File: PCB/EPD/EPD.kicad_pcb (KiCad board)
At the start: 2 copper layers, 70 x 70 mm, 66 parts, among them J1 Conn_01x26, J2 Shelly, J3 USB-PROG, J4 BTN1, J6 BTN2, J7 USB-C-Socket-V, J8 PWR, P1 +, P10 2, P11 1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

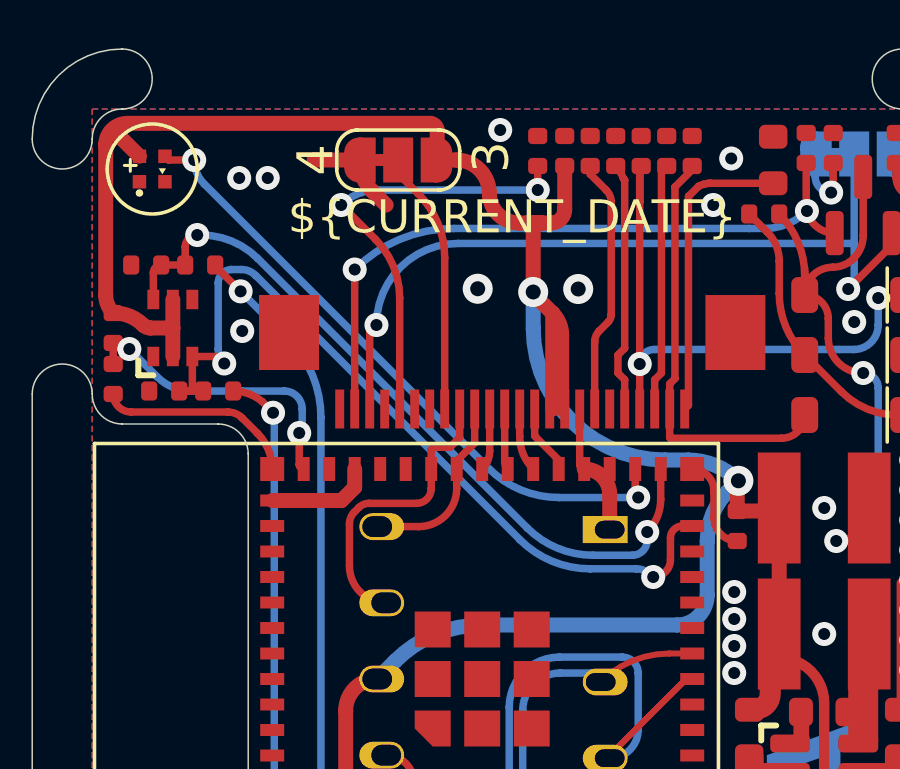
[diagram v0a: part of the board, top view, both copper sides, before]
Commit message: Moved connector and tidy GPIOs used
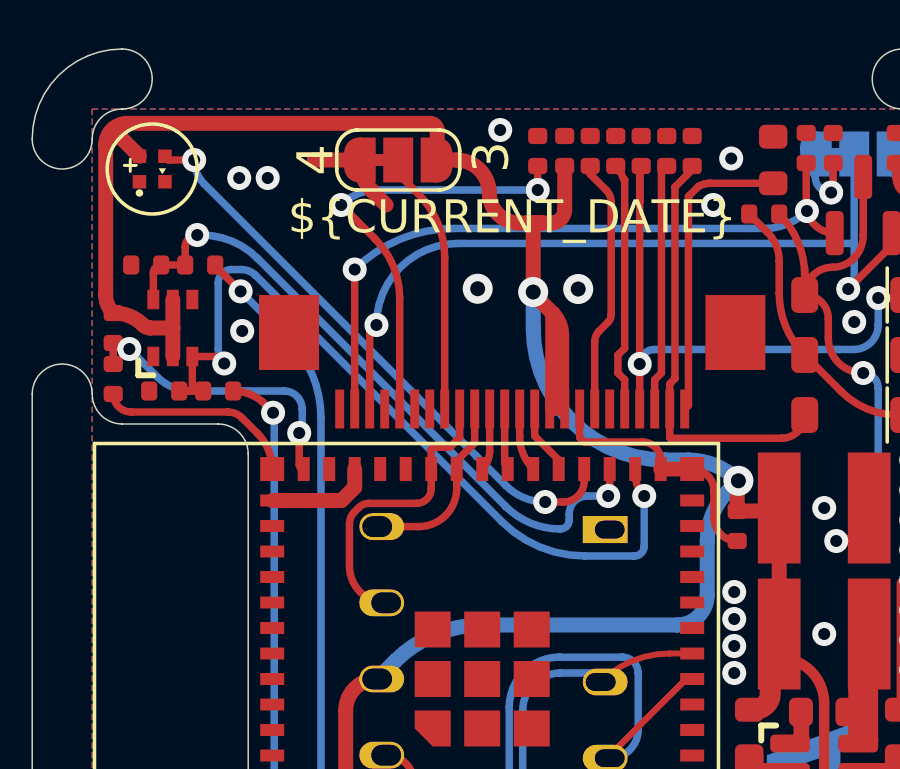
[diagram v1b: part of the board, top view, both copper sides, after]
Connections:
- U4 pad 29: BTN1 -> unconnected-(U4-GPIO34-Pad29)
- U4 pad 31: BTN2 -> GND
- U4 pad 32: RGB -> BTN1
- U4 pad 33: GND -> BTN2
- U4 pad 34: GND -> RGB
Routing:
- net BTN2: track 25.2 -> 22.4 mm
- net RGB: track 21.5 -> 19.6 mm
- net GND: track 21.3 -> 22.1 mm
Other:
- board text added: "43"
- board text added: "44"
- board text removed: "34"
- board text removed: "35"

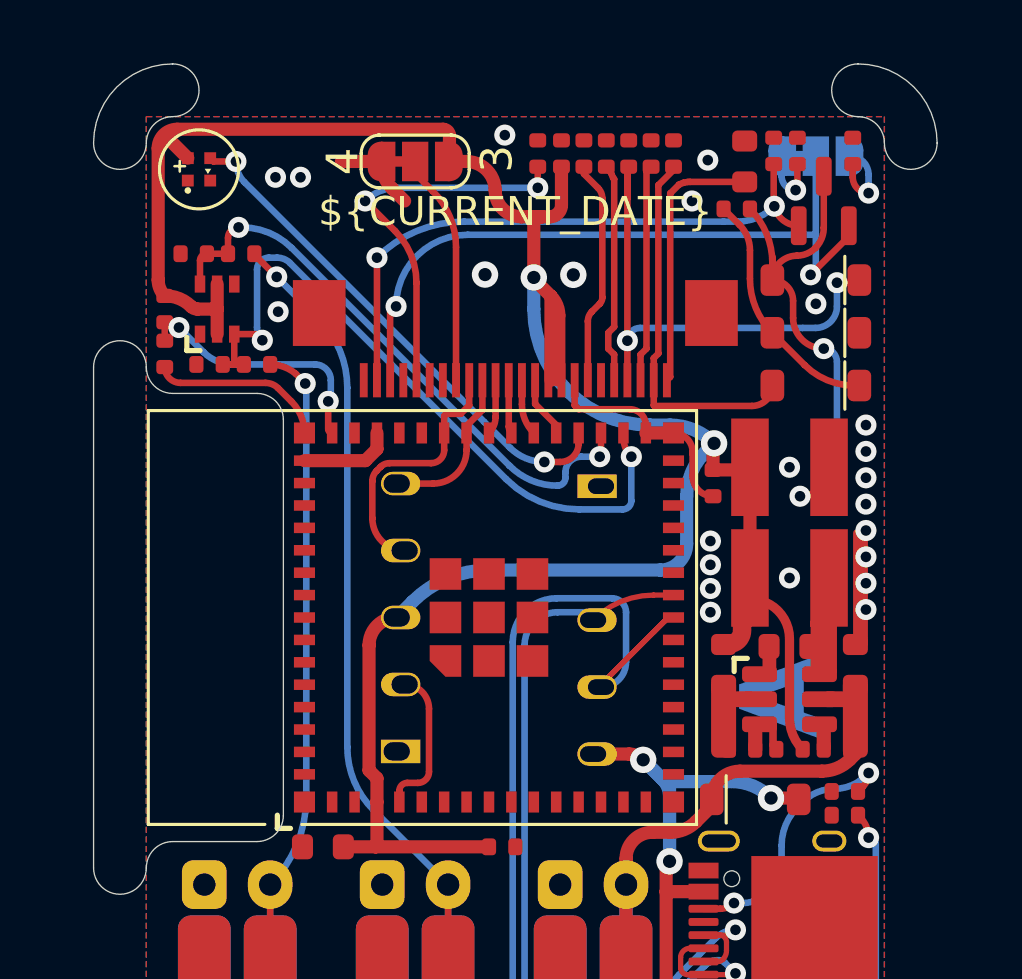
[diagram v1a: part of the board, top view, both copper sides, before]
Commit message: Moved connector to reduce slack
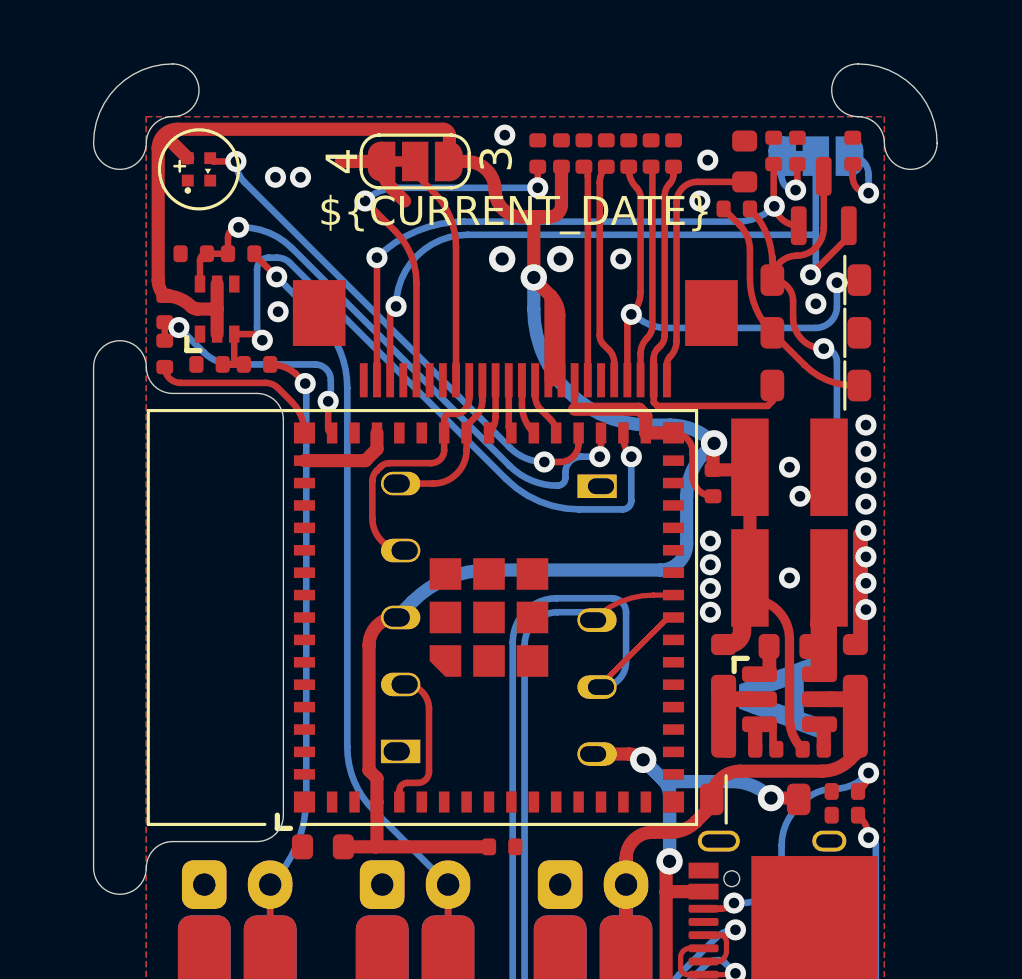
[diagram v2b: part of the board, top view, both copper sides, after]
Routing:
- net GND: track 22.1 -> 25.6 mm, vias 23 -> 24
- net Net-(D3-K): track 19.6 -> 18.2 mm
- net Net-(D2-A): track 14.2 -> 15.1 mm

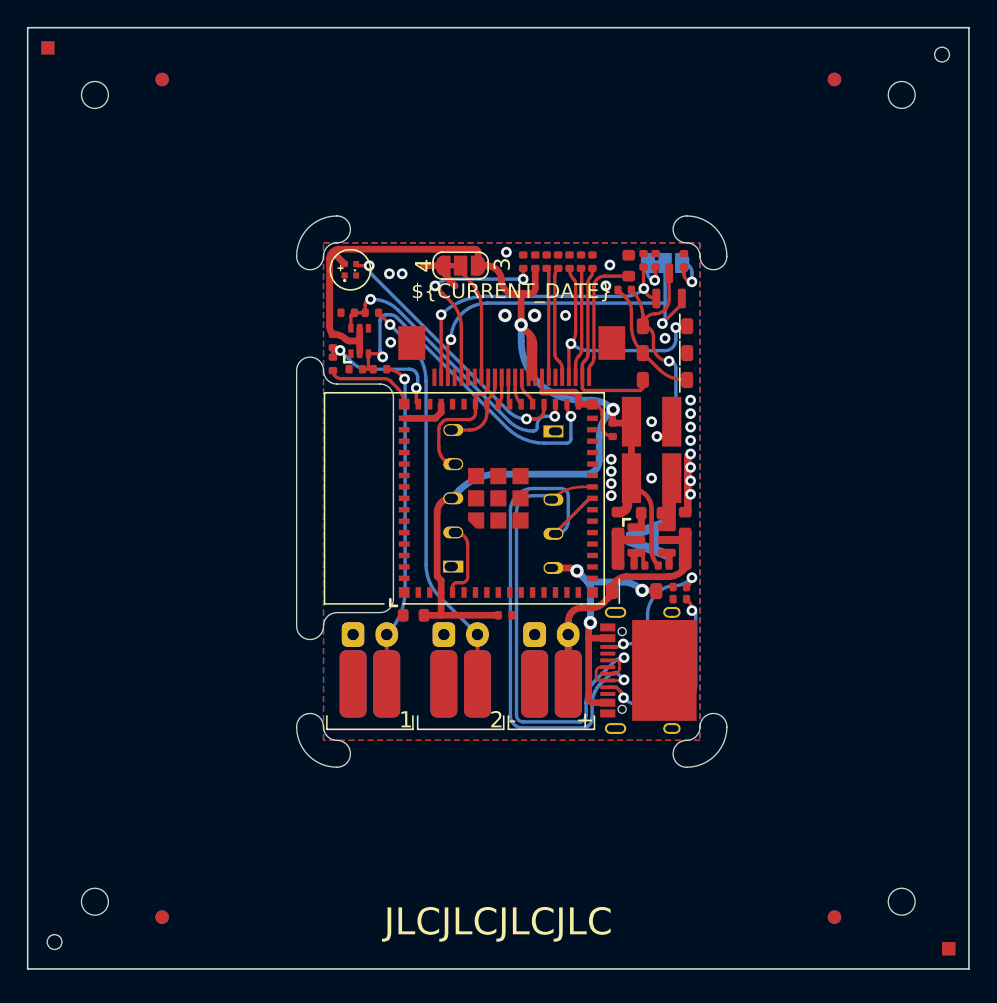
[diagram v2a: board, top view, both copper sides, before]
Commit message: Changed ESD
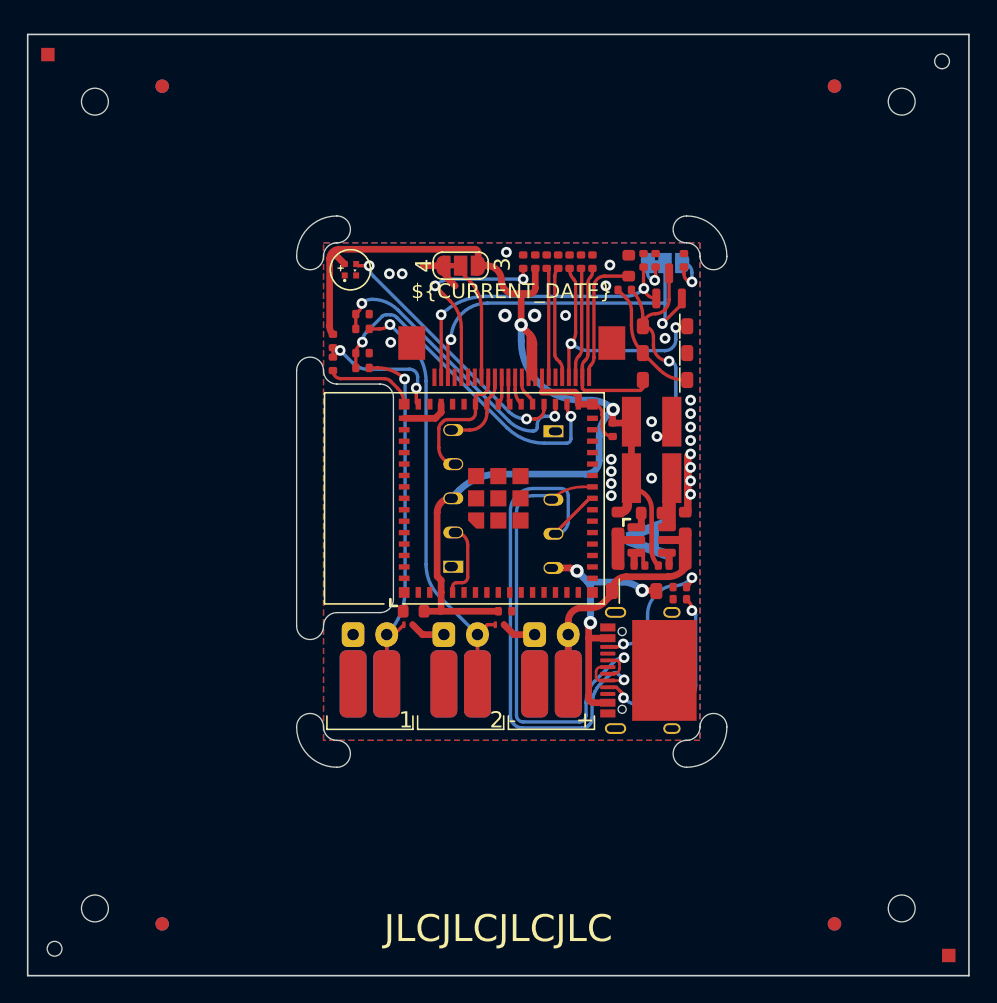
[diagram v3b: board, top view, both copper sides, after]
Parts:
- removed C22: 33pF, RevK:C_0402
- added C19: 33pF, RevK:C_0402, F.Cu at (88.9, 79.2)
- added D5: ~, RevK:DFN1006-2L, F.Cu at (99.1, 99.4)
- D7: value BAV99S -> ~; footprint RevK:SOT-363_SC-70-6 -> RevK:DFN1006-2L
- J4: value BTN1 -> BTN2
- P11, P12, P5, P6: value 1 -> 2
- moved D7 21.4 mm to (92.3, 99.4), turned to 180 degrees
- moved R6 1.39 mm to (88.9, 77.4)
- moved R7 1.30 mm to (88.9, 80.3)
- moved C21 1.10 mm to (88.9, 76.3), turned to 0 degrees
- moved PCB1 0.50 mm to (99.0, 90.5)
- moved C2 0.30 mm to (99.5, 98.4)
- moved C5 0.30 mm to (92.7, 98.4)
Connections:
- D7 pad 2: +3.3V -> Net-(J4-Pin_2)
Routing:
- net GND: track 25.6 -> 30.8 mm
- net +3.3V: track 88.7 -> 84.4 mm
- net Net-(J4-Pin_2): track 28.3 -> 30.6 mm
- net Net-(J6-Pin_2): track 33.9 -> 36.0 mm
- net BTN1: track 26.7 -> 25.0 mm
- net Net-(D3-A): track 20.7 -> 19.8 mm
- net BTN2: track 22.4 -> 21.8 mm

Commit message: Caps, etc.
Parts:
- moved D6 0.14 mm to (109.0, 97.0), turned to -10 degrees
